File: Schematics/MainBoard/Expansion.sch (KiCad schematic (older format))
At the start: 6 parts, among them J16 Device 2, J17 Device 5, J18 Device 3, J19 Device 6, J20 Device 4, J21 Device 7

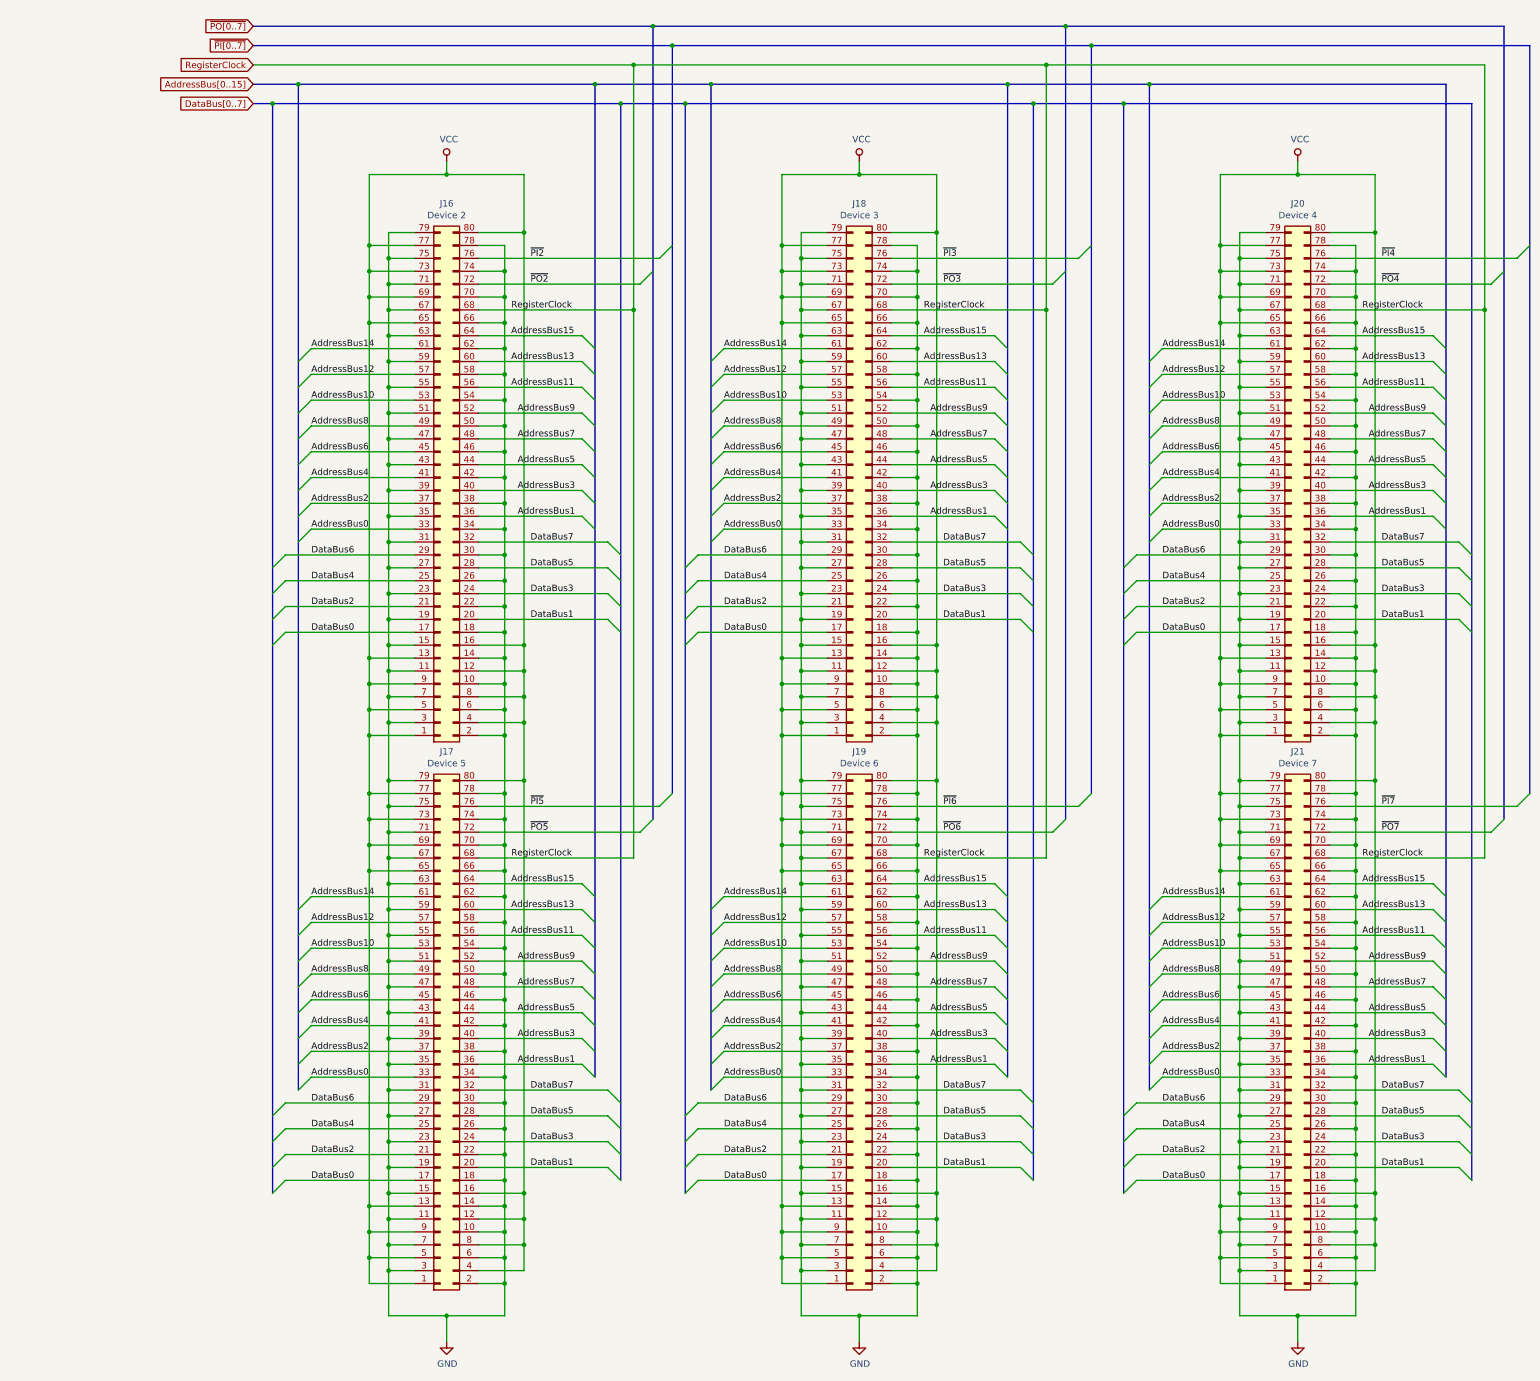
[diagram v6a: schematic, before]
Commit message: Add /RST and ControlClock to the expansion connector.
The Reset signal will definitely be useful. The ControlClock signal might
be, but I don't know what for yet. Fortunately, there are plenty of unused
pins here.
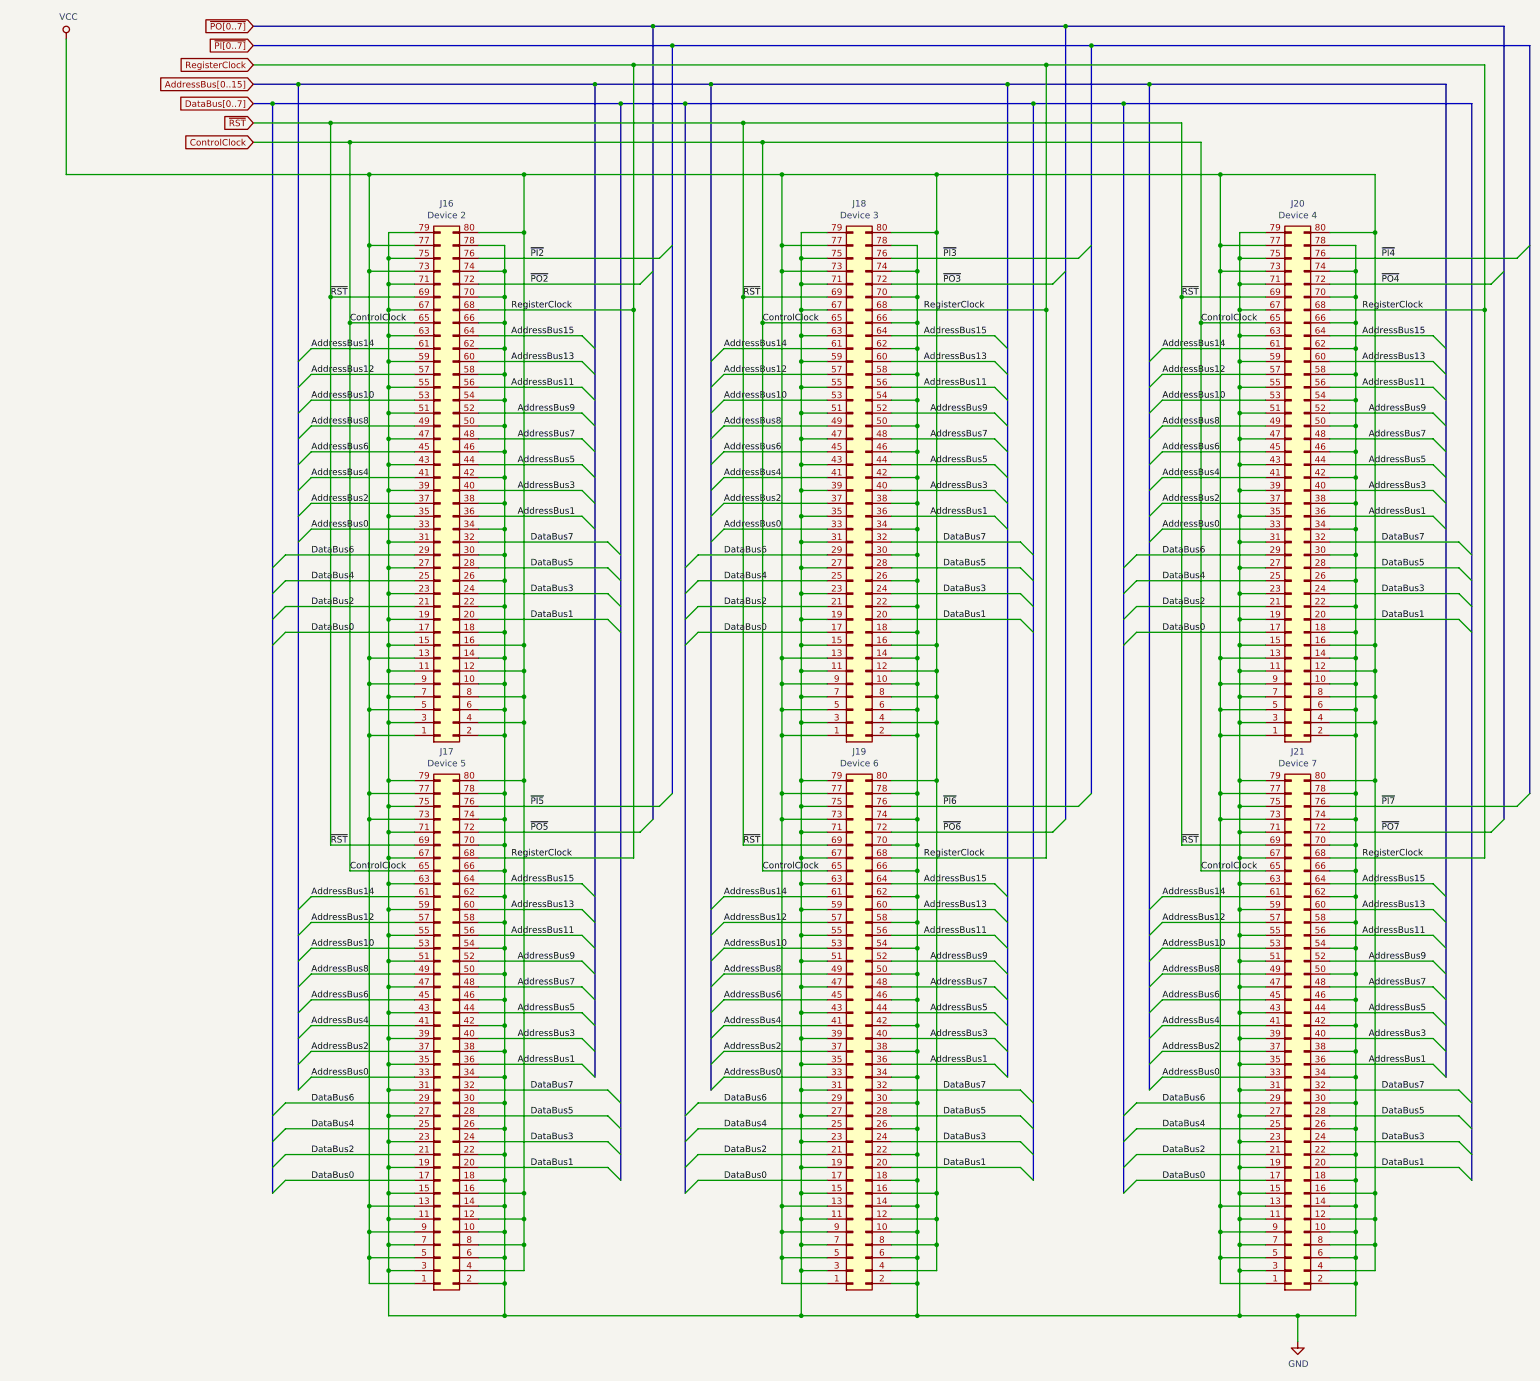
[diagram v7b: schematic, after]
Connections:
- net VCC: no longer J16.65 (Pin_65), J16.69 (Pin_69), J17.65 (Pin_65), J17.69 (Pin_69), J18.65 (Pin_65), J18.69 (Pin_69), J19.65 (Pin_65), J19.69 (Pin_69), J20.65 (Pin_65), J20.69 (Pin_69), J21.65 (Pin_65), J21.69 (Pin_69)
- new net ControlClock: J16.65 (Pin_65), J17.65 (Pin_65), J18.65 (Pin_65), J19.65 (Pin_65), J20.65 (Pin_65), J21.65 (Pin_65)
- new net ~RST: J16.69 (Pin_69), J17.69 (Pin_69), J18.69 (Pin_69), J19.69 (Pin_69), J20.69 (Pin_69), J21.69 (Pin_69)
